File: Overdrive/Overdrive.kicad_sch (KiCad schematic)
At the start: 49 parts, among them J1 DC IN, J2 9V battery, J4 IN, J5 OUT, Q1 MMBT2222A, Q2 MMBT2222A, U1 TL072, U2 TL072

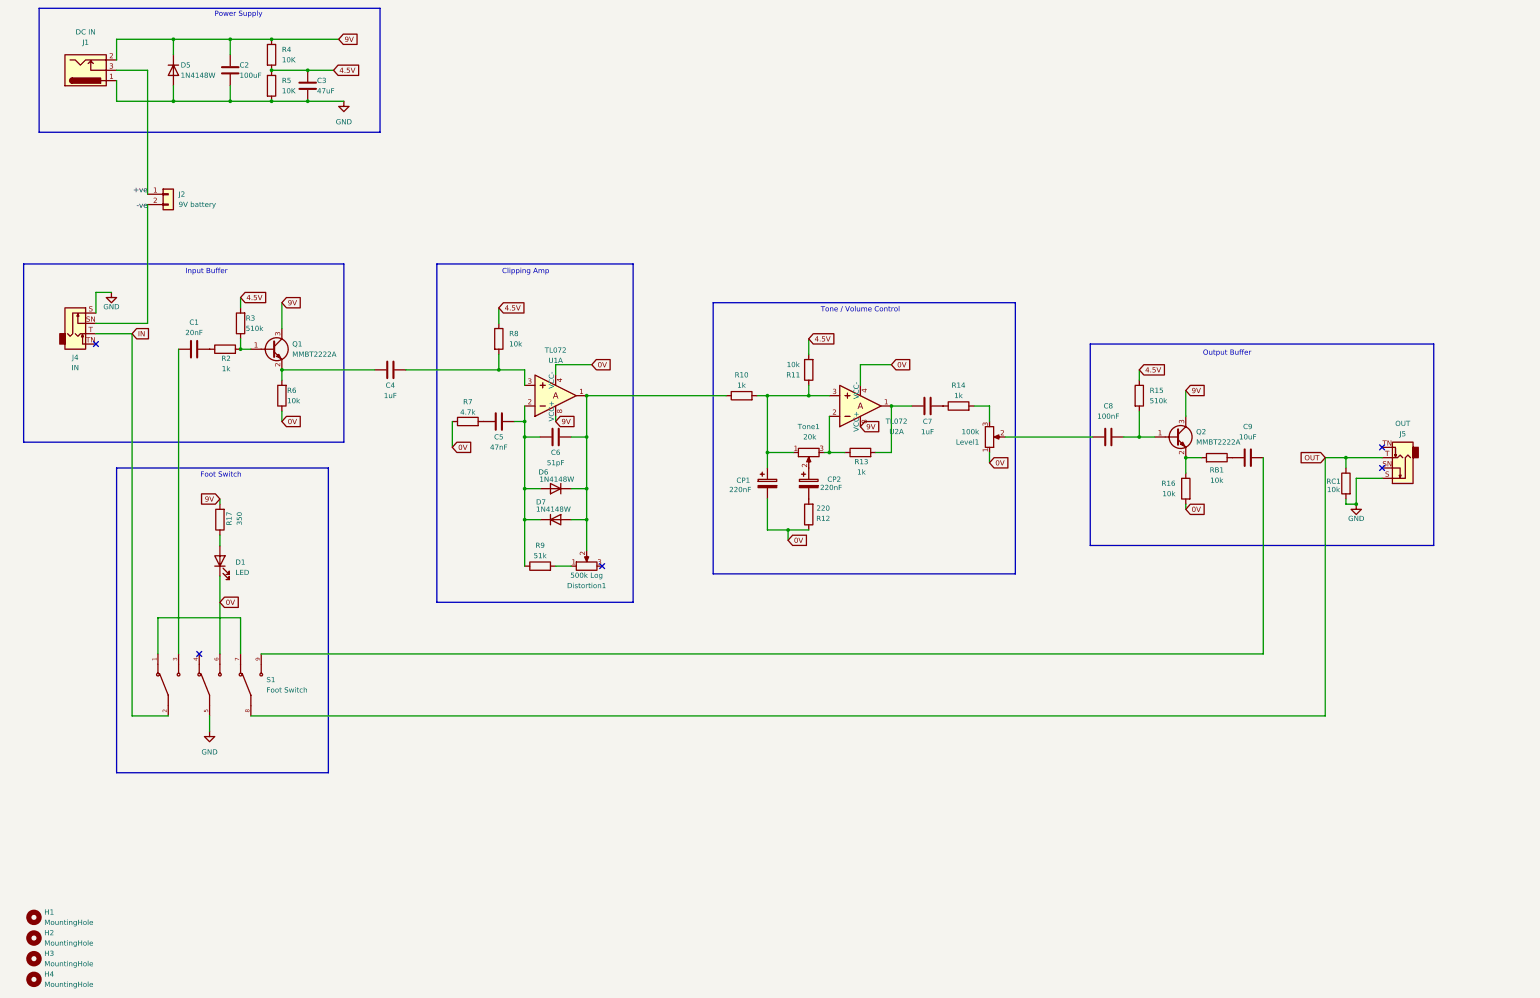
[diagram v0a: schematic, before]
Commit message: Redesigned PCB layout to be 110mm x 60mm
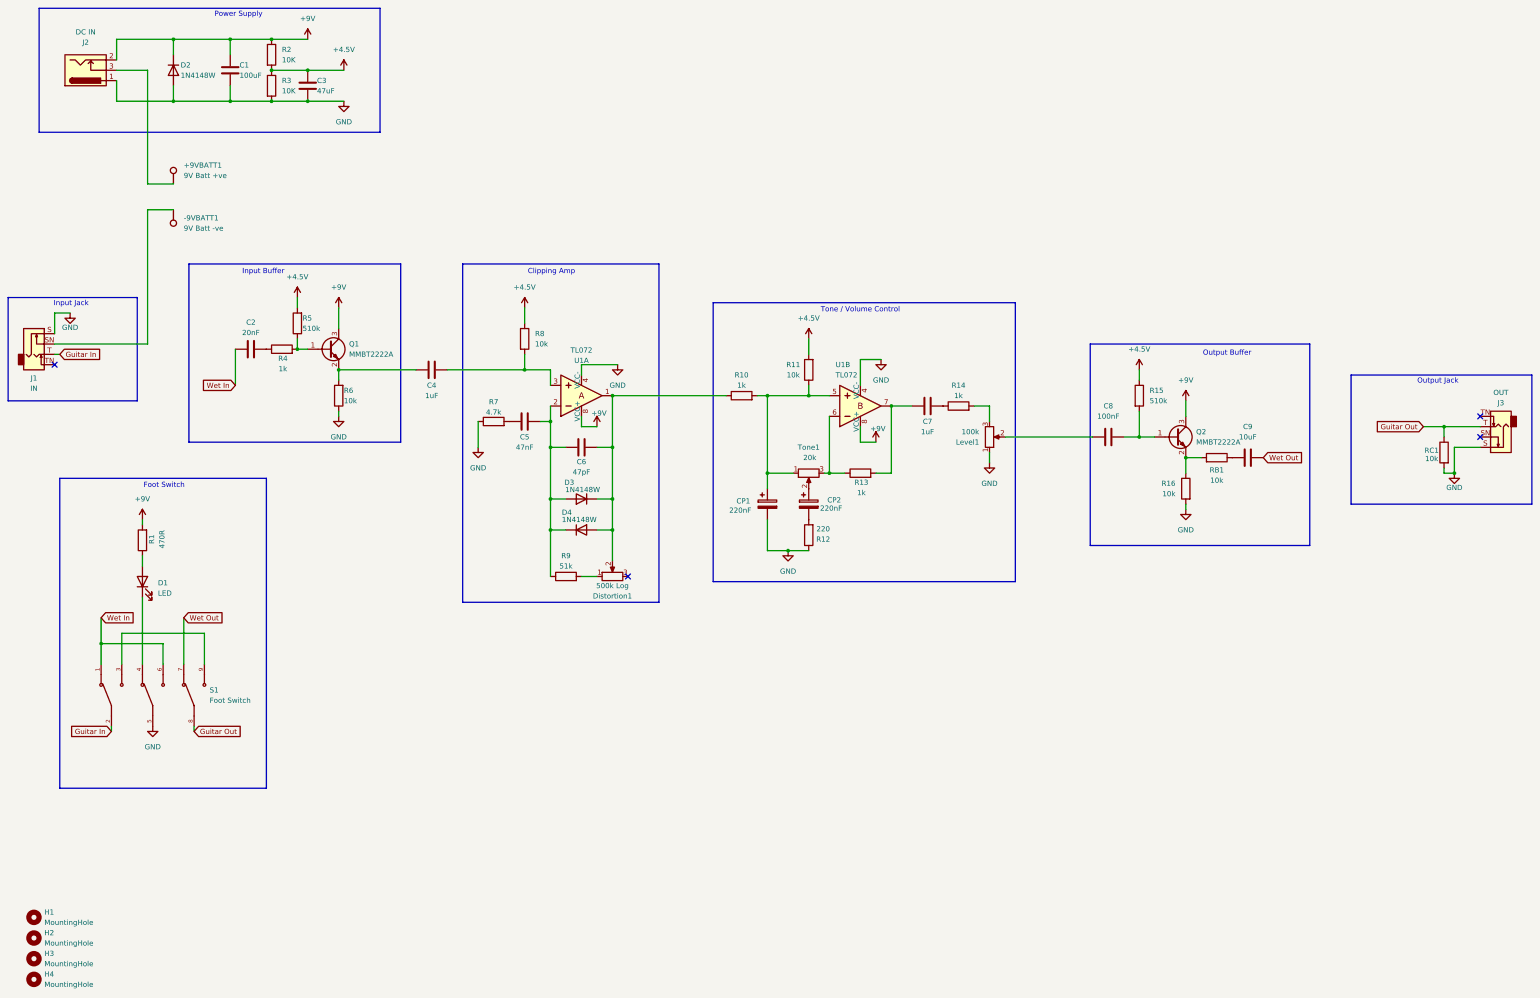
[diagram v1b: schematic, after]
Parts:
- removed J2: 9V battery, Connector_PinSocket_2.00mm:PinSocket_1x02_P2.00mm_Vertical, symbol Connector_Generic:Conn_01x02
- removed U2: TL072, Package_SO:SOIC-8_3.9x4.9mm_P1.27mm, symbol dk_Linear-Amplifiers-Instrumentation-OP-Amps-Buffer-Amps:TL072CP
- added +9VBATT1: 9V Batt +ve, TestPoint:TestPoint_THTPad_2.5x2.5mm_Drill1.2mm, symbol Connector:TestPoint
- added -9VBATT1: 9V Batt -ve, TestPoint:TestPoint_THTPad_2.5x2.5mm_Drill1.2mm, symbol Connector:TestPoint
- added unit 1 of U1
- C3: footprint Capacitor_SMD:C_0805_2012Metric -> Capacitor_SMD:C_1206_3216Metric
- C6: value 51pF -> 47pF
- CP1, CP2: footprint Capacitor_SMD:C_0603_1608Metric -> Capacitor_SMD:CP_Elec_3x5.4
- R1: renamed from R17; value 350 -> 470R
- renumbered C2 to C1, C1 to C2, D5 to D2, D6 to D3, D7 to D4, J4 to J1, J1 to J2, J5 to J3, R4 to R2, R5 to R3, R2 to R4, R3 to R5
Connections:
- net GND: now also CP1.2, Level1.1, R12.1, R16.2, R6.1, R7.1, U1.4 (VCC-), U1.4 (VCC-)
- net at C5.2, C6.1, D3.2 (A)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: now also U1.2; no longer U1.2
- net at C6.2, D3.1 (K), D4.2 (A)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: now also U1.1; no longer U1.1
- net at CP1.1, R10.2, R11.1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: now also U1.5
- net at C4.2, R8.2: now also U1.3; no longer U1.3
- net at S1.3: now also S1.9; no longer C2.1
- net at R13.1, Tone1.3: now also U1.6
- net at C7.1, R13.2: now also U1.7
- net Wet Out: now reaches C9.2
- net Wet Out: now also S1.7; no longer S1.9
- net Wet In: now reaches S1.1
- net Wet In: now also C2.1, S1.6; no longer S1.7
- net at S1.4: now also D1.1 (K)
- net +ve: no longer names the net of J2.3
- net +ve: now also +9VBATT1.1
- net -ve: no longer names the net of J1.SN
- net -ve: now also -9VBATT1.1
- removed net 0V: CP1.2, D1.1 (K), Level1.1, R12.1, R16.2, R6.1, R7.1, S1.6, U1.4 (VCC-)
- net 4.5V renamed +4.5V
- net 9V renamed +9V
- net +9V: now also U1.8 (VCC+)
- net IN renamed Guitar In
- net OUT renamed Guitar Out
- no-connect marks 5 -> 4
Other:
- note added: "Input Jack"
- note added: "Output Jack"
- moved on the sheet: C2, C4, C5, C6, CP1, CP2, D3, D4, Distortion1, J1, J3, Q1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

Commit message: added hard clipping switch, changed electrolytic caps to be THT and to be sources separately.
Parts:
- added SW1: SW_SPDT, Button_Switch_THT:spdt switch custom, symbol Switch:SW_SPDT
- CP1, CP2: footprint Capacitor_SMD:CP_Elec_3x5.4 -> Capacitor_THT:CP_Radial_D5.0mm_P2.50mm
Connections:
- net GND: now also SW1.1 (A)
- net at C5.2, C6.1, R9.1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: now also SW1.3 (C); no longer D3.2 (A), D4.1 (K)
- new net: D3.2 (A), D4.1 (K), SW1.2 (B)
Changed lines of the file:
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@@
 	)
 	(junction
-		(at 152.4 165.1)
-		(diameter 0)
-		(color 0 0 0 0)
-	)
-	(junction
 		(at 210.82 170.18)
 		(diameter 0)
@@
 	)
 	(junction
+		(at 142.24 158.75)
+		(diameter 0)
+		(color 0 0 0 0)
+	)
+	(junction
 		(at 59.69 59.69)
 		(diameter 0)
@@
 	)
 	(junction
-		(at 152.4 157.48)
+		(at 154.94 161.29)
 		(diameter 0)
 		(color 0 0 0 0)
@@
 	(wire
 		(pts
-			(xy 156.21 165.1) (xy 152.4 165.1)
-		)
-		(stroke
-			(width 0)
-			(type default)
-		)
-	)
-	(wire
-		(pts
 			(xy 92.71 120.65) (xy 90.17 120.65)
 		)
@@
 	(wire
 		(pts
-			(xy 160.02 139.7) (xy 163.83 139.7)
+			(xy 142.24 144.78) (xy 142.24 158.75)
 		)
 		(stroke
@@
 	(wire
 		(pts
-			(xy 100.33 125.73) (xy 100.33 128.27)
+			(xy 154.94 161.29) (xy 154.94 157.48)
 		)
 		(stroke
@@
 	(wire
 		(pts
-			(xy 41.91 198.12) (xy 41.91 193.04)
+			(xy 160.02 139.7) (xy 163.83 139.7)
 		)
 		(stroke
@@
 	(wire
 		(pts
-			(xy 152.4 134.62) (xy 152.4 138.43)
+			(xy 100.33 125.73) (xy 100.33 128.27)
 		)
 		(stroke
@@
 	(wire
 		(pts
-			(xy 163.83 165.1) (xy 167.64 165.1)
+			(xy 41.91 198.12) (xy 41.91 193.04)
 		)
 		(stroke
@@
 	(wire
 		(pts
-			(xy 45.72 44.45) (xy 59.69 44.45)
+			(xy 152.4 134.62) (xy 152.4 138.43)
 		)
 		(stroke
@@
 	(wire
 		(pts
-			(xy 152.4 157.48) (xy 152.4 144.78)
+			(xy 163.83 165.1) (xy 167.64 165.1)
 		)
 		(stroke
@@
 	(wire
 		(pts
-			(xy 210.82 170.18) (xy 215.9 170.18)
+			(xy 45.72 44.45) (xy 59.69 44.45)
 		)
 		(stroke
@@
 	(wire
 		(pts
-			(xy 90.17 118.11) (xy 90.17 120.65)
+			(xy 210.82 170.18) (xy 215.9 170.18)
 		)
 		(stroke
@@
 	(wire
 		(pts
-			(xy 212.09 151.13) (xy 205.74 151.13)
+			(xy 90.17 118.11) (xy 90.17 120.65)
 		)
 		(stroke
@@
 	(wire
 		(pts
-			(xy 372.11 139.7) (xy 372.11 142.24)
+			(xy 212.09 151.13) (xy 205.74 151.13)
 		)
 		(stroke
@@
 	(wire
 		(pts
-			(xy 152.4 165.1) (xy 152.4 157.48)
+			(xy 372.11 139.7) (xy 372.11 142.24)
 		)
 		(stroke
@@
 	(wire
 		(pts
-			(xy 156.21 157.48) (xy 152.4 157.48)
-		)
-		(stroke
-			(width 0)
-			(type default)
-		)
-	)
-	(wire
-		(pts
 			(xy 52.07 171.45) (xy 52.07 173.99)
 		)
@@
 	(wire
 		(pts
+			(xy 142.24 158.75) (xy 142.24 176.53)
+		)
+		(stroke
+			(width 0)
+			(type default)
+		)
+	)
+	(wire
+		(pts
 			(xy 59.69 44.45) (xy 73.66 44.45)
 		)
@@
 	(wire
 		(pts
+			(xy 154.94 165.1) (xy 154.94 161.29)
+		)
+		(stroke
+			(width 0)
+			(type default)
+		)
+	)
+	(wire
+		(pts
 			(xy 236.22 151.13) (xy 236.22 134.62)
 		)
@@
 	(wire
 		(pts
+			(xy 142.24 176.53) (xy 152.4 176.53)
+		)
+		(stroke
+			(width 0)
+			(type default)
+		)
+	)
+	(wire
+		(pts
 			(xy 73.66 55.88) (xy 73.66 59.69)
 		)
@@
 	(wire
 		(pts
-			(xy 152.4 165.1) (xy 152.4 176.53)
+			(xy 142.24 158.75) (xy 144.78 158.75)
 		)
 		(stroke
@@
 	(wire
 		(pts
+			(xy 154.94 157.48) (xy 156.21 157.48)
+		)
+		(stroke
+			(width 0)
+			(type default)
+		)
+	)
+	(wire
+		(pts
 			(xy 59.69 59.69) (xy 73.66 59.69)
 		)
@@
 	(wire
 		(pts
+			(xy 142.24 144.78) (xy 152.4 144.78)
+		)
+		(stroke
+			(width 0)
+			(type default)
+		)
+	)
+	(wire
+		(pts
 			(xy 167.64 165.1) (xy 167.64 157.48)
 		)
@@
 	(wire
 		(pts
+			(xy 156.21 165.1) (xy 154.94 165.1)
+		)
+		(stroke
+			(width 0)
+			(type default)
+		)
+	)
+	(wire
+		(pts
 			(xy 53.34 119.38) (xy 30.48 119.38)
 		)
@@
 	)
 	(symbol
+		(lib_id "power:GND")
+		(at 144.78 163.83 0)
+		(unit 1)
+		(exclude_from_sim no)
+		(in_bom yes)
+		(on_board yes)
+		(dnp no)
+		(fields_autoplaced yes)
+		(property "Reference" "#PWR023"
+			(at 144.78 170.18 0)
+			(effects
+				(font
+					(size 1.27 1.27)
+				)
+				(hide yes)
+			)
+		)
+		(property "Value" "GND"
+			(at 144.78 168.91 0)
+			(effects
+				(font
+					(size 1.27 1.27)
+				)
+			)
+		)
+		(property "Footprint" ""
+			(at 144.78 163.83 0)
+			(effects
+				(font
+					(size 1.27 1.27)
+				)
+				(hide yes)
+			)
+		)
+		(property "Datasheet" ""
+			(at 144.78 163.83 0)
+			(effects
+				(font
+					(size 1.27 1.27)
+				)
+				(hide yes)
+			)
+		)
+		(property "Description" "Power symbol creates a global label with name \"GND\" , ground"
+			(at 144.78 163.83 0)
+			(effects
+				(font
+					(size 1.27 1.27)
+				)
+				(hide yes)
+			)
+		)
+		(pin "1"
+		)
+		(instances
+			(project "Overdrive"
+				(path "/11b95356-caa1-437c-a82a-3070bdc35e65"
+					(reference "#PWR023")
+					(unit 1)
+				)
+			)
+		)
+	)
+	(symbol
 		(lib_id "Diode:1N4148W")
 		(at 160.02 165.1 0)
@@
 	)
 	(symbol
+		(lib_id "Switch:SW_SPDT")
+		(at 149.86 161.29 180)
+		(unit 1)
+		(exclude_from_sim no)
+		(in_bom yes)
+		(on_board yes)
+		(dnp no)
+		(fields_autoplaced yes)
+		(property "Reference" "SW1"
+			(at 149.86 152.4 0)
+			(effects
+				(font
+					(size 1.27 1.27)
+				)
+			)
+		)
+		(property "Value" "SW_SPDT"
+			(at 149.86 154.94 0)
+			(effects
+				(font
+					(size 1.27 1.27)
+				)
+			)
+		)
+		(property "Footprint" "Button_Switch_THT:spdt switch custom"
+			(at 149.86 161.29 0)
+			(effects
+				(font
+					(size 1.27 1.27)
+				)
+				(hide yes)
+			)
+		)
+		(property "Datasheet" "~"
+			(at 149.86 153.67 0)
+			(effects
+				(font
+					(size 1.27 1.27)
+				)
+				(hide yes)
+			)
+		)
+		(property "Description" "Switch, single pole double throw"
+			(at 149.86 161.29 0)
+			(effects
+				(font
+					(size 1.27 1.27)
+				)
+				(hide yes)
+			)
+		)
+		(pin "3"
+		)
+		(pin "2"
+		)
+		(pin "1"
+		)
+		(instances
+			(project ""
+				(path "/11b95356-caa1-437c-a82a-3070bdc35e65"
+					(reference "SW1")
+					(unit 1)
+				)
+			)
+		)
+	)
+	(symbol
 		(lib_id "power:GND")
 		(at 168.91 124.46 0)
@@
 			)
 		)
-		(property "Footprint" "Capacitor_SMD:CP_Elec_3x5.4"
+		(property "Footprint" "Capacitor_THT:CP_Radial_D5.0mm_P2.50mm"
 			(at 206.7052 162.56 0)
 			(effects
@@
 			)
 		)
-		(property "Footprint" "Capacitor_SMD:CP_Elec_3x5.4"
+		(property "Footprint" "Capacitor_THT:CP_Radial_D5.0mm_P2.50mm"
 			(at 216.8652 162.56 0)
 			(effects
@@
 		(dnp no)
 		(property "Reference" "C5"
-			(at 146.05 142.24 90)
+			(at 146.05 132.588 90)
 			(effects
 				(font
@@
 		)
 		(property "Value" "47nF"
-			(at 146.05 144.78 90)
+			(at 146.05 135.128 90)
 			(effects
 				(font
